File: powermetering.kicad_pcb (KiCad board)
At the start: 2 copper layers, 194 x 114.1 mm, 226 parts, among them J1 Conn_01x04, J16 Conn_02x20_Odd_Even, J2 Conn_01x02, J3 Conn_01x02, J4 Conn_01x02, J5 Conn_01x02, J6 HY951180A_RJ45, J7 CONN_01X02, J9 CONN_01X02, P2 CONN_01X04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

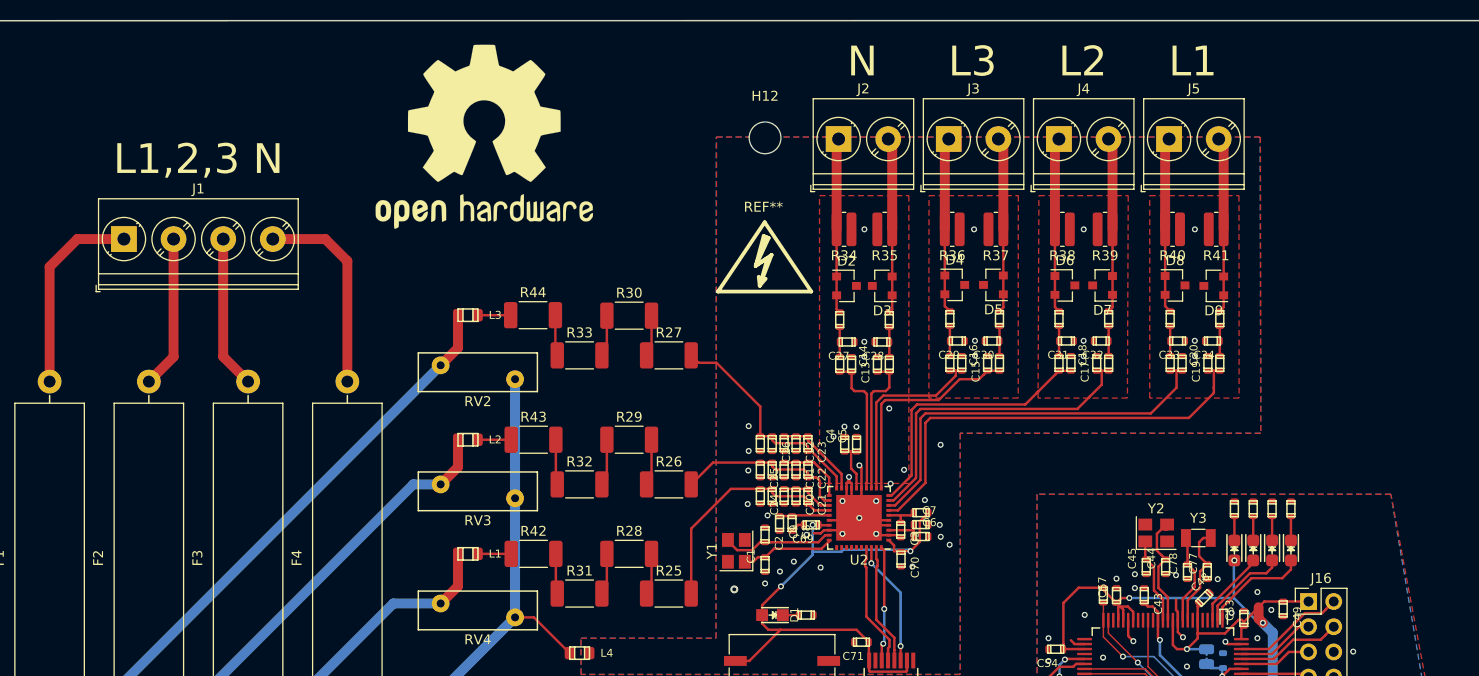
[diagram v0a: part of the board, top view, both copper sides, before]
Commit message: add EMI capacitor
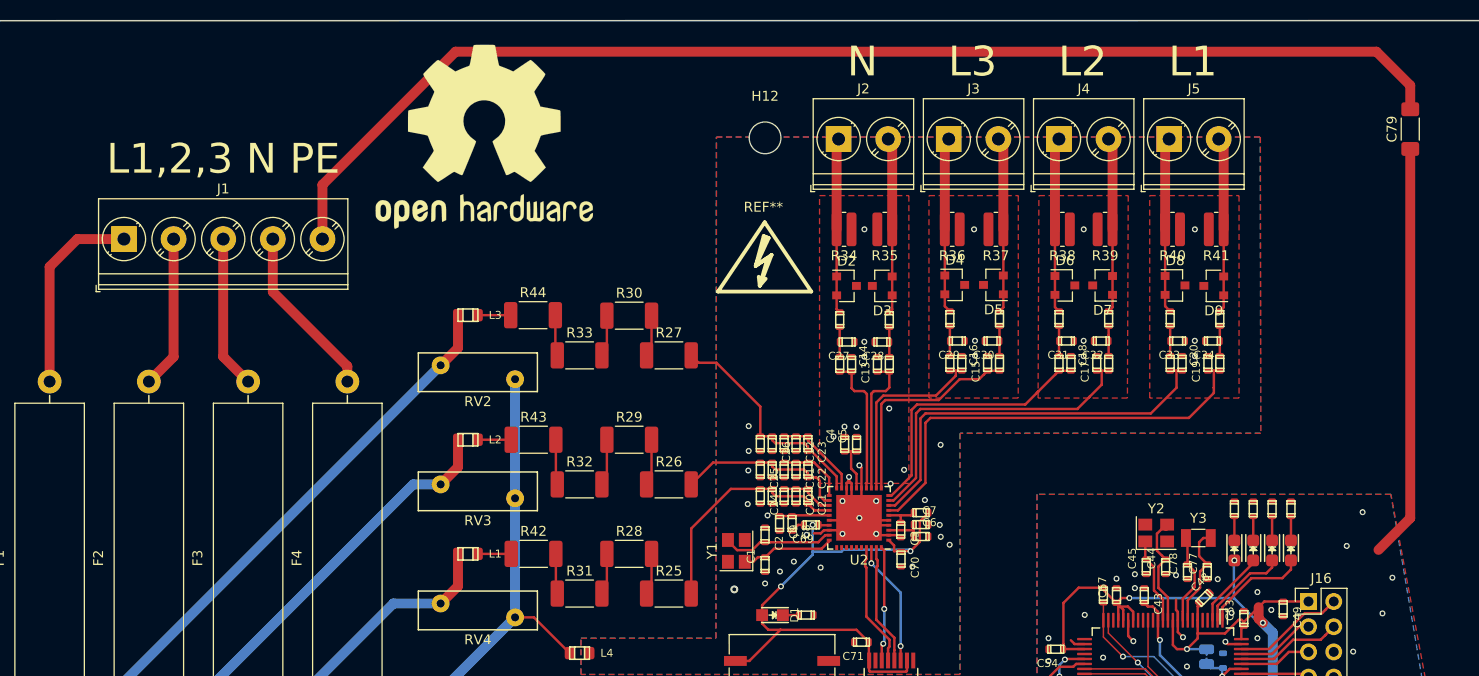
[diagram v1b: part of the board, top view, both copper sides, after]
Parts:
- added C79: C, Capacitor_SMD:C_1806_4516Metric, F.Cu at (265.0, 63.4)
- J1: footprint TerminalBlock_Phoenix:TerminalBlock_Phoenix_PT-1,5-4-5.0-H_1x04_P5.00mm_Horizontal -> TerminalBlock_Phoenix:TerminalBlock_Phoenix_PT-1,5-5-5.0-H_1x05_P5.00mm_Horizontal
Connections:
- net /phy_plug/PHY_CRS renamed /PHY_CRS
- net /phy_plug/PHY_INTRP renamed /PHY_INTRP
- net /phy_plug/PHY_MDC renamed /STM_MDC
- net /phy_plug/PHY_MDIO renamed /STM_MDIO
- net /phy_plug/PHY_REFCLK renamed /PHY_REFCLK
- net /phy_plug/PHY_RST renamed /PHY_RST
- net /phy_plug/PHY_RXD0 renamed /STM_RXD0
- net /phy_plug/PHY_RXD1 renamed /STM_RXD1
- net /phy_plug/PHY_TXD0 renamed /PHY_TXD0
- net /phy_plug/PHY_TXD1 renamed /STM_TXD1
- net /phy_plug/PHY_TXEN renamed /STM_TXEN
- net /phy_plug/PHY_X0 renamed /PHY_X0
- net /phy_plug/PHY_XI renamed /PHY_XI
- net /stm32/STM_MCO0 renamed /STM_MCO0
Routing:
- net Earth_Protective: track 0.00 -> 124.4 mm
- net GND: track 17.4 -> 59.2 mm, vias 92 -> 96
- net Net-(F4-Pad1): track 20.6 -> 17.5 mm
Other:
- board text added: "L1,2,3 N PE"
- board text removed: "L1,2,3 N"

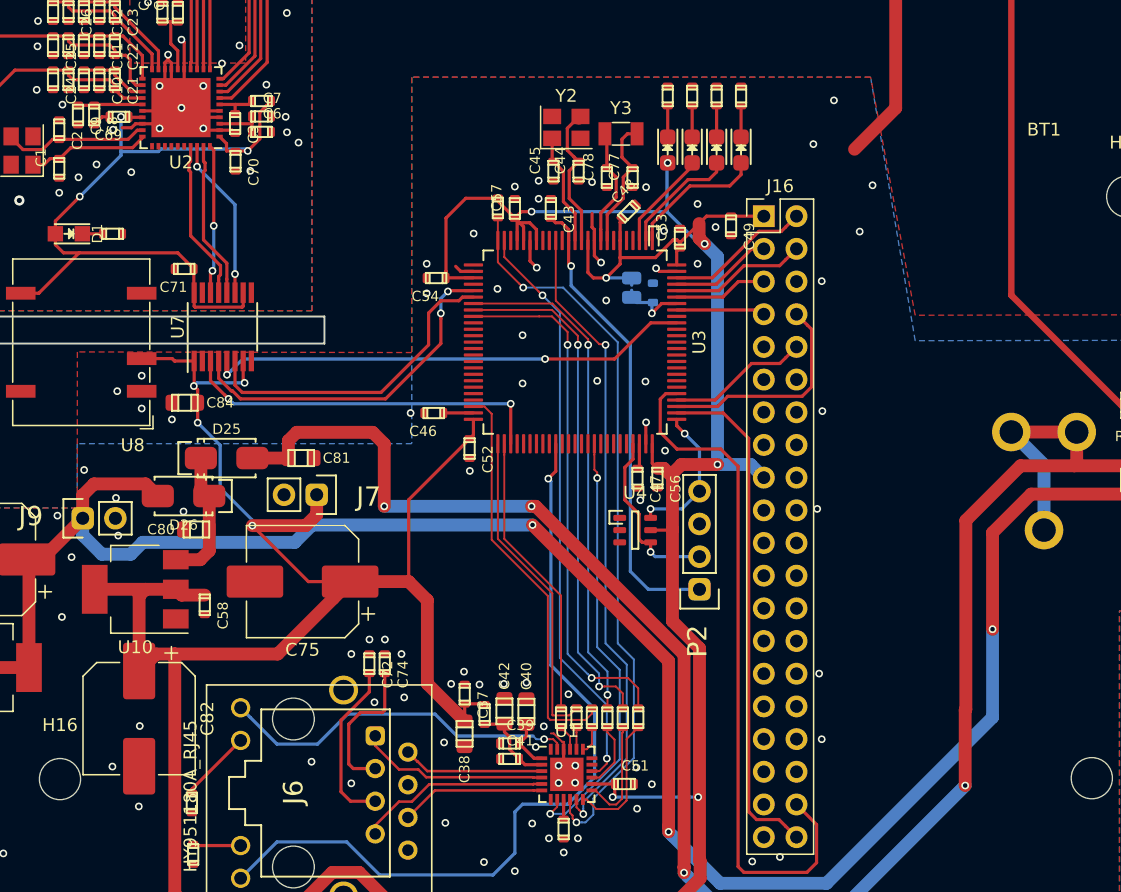
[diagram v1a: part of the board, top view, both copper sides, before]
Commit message: add sd card holder
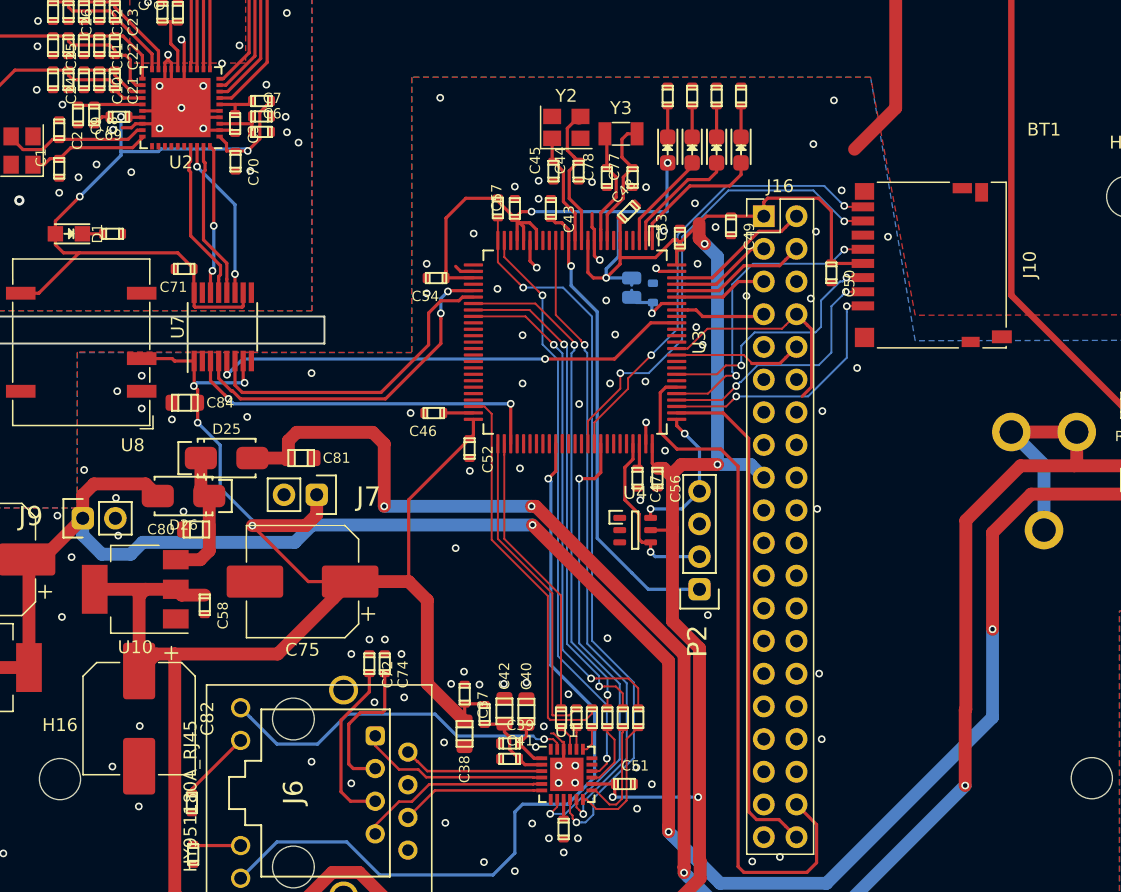
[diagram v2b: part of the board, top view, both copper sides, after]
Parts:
- added C50: 100n, stmbl:C_0603, F.Cu at (260.0, 115.4)
- added J10: Micro_SD_Card, Connector_Card:microSD_HC_Hirose_DM3D-SF, F.Cu at (267.8, 114.8)
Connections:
- net /PHY_REFCLK renamed /STM_REFCLK
- U1 pad 8: /PHY_XI -> /STM_MCO0
- U3 pad 66: /PHY_XI -> Net-(J10-Pad8)
- U3 pad 78: USART3_TX -> Net-(J10-Pad1)
- U3 pad 79: USART3_RX -> Net-(J10-Pad2)
- U3 pad 80: MMDVM_BOOT0 -> Net-(J10-Pad5)
- U3 pad 81: Net-(U3-Pad81) -> MMDVM_BOOT0
- U3 pad 86: Net-(U3-Pad86) -> USART3_RX
- U3 pad 87: Net-(U3-Pad87) -> USART3_TX
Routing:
- net Net-(J10-Pad7): track 0.00 -> 37.0 mm, vias 0 -> 2
- net /STM_MCO0: track 0.00 -> 35.7 mm, vias 0 -> 2
- net Net-(J10-Pad8): track 0.00 -> 35.6 mm, vias 0 -> 2
- net /PHY_XI: track 33.8 -> 0.00 mm, vias 2 -> 0
- net Net-(J10-Pad5): track 0.00 -> 23.7 mm, vias 0 -> 2
- net Net-(J10-Pad2): track 0.00 -> 20.1 mm, vias 0 -> 2
- net Net-(J10-Pad1): track 0.00 -> 20.1 mm, vias 0 -> 2
- net Net-(J10-Pad3): track 0.00 -> 19.7 mm, vias 0 -> 2
- net +3V3: track 313.1 -> 328.6 mm
- net /STM_RXD1: track 41.0 -> 39.8 mm
- net /STM_RXD0: track 40.1 -> 39.1 mm
- net USART3_RX: track 11.0 -> 10.1 mm
- net /PHY_CRS: track 39.4 -> 38.8 mm
- net MMDVM_BOOT0: track 54.1 -> 54.6 mm
- net GND: vias 96 -> 110

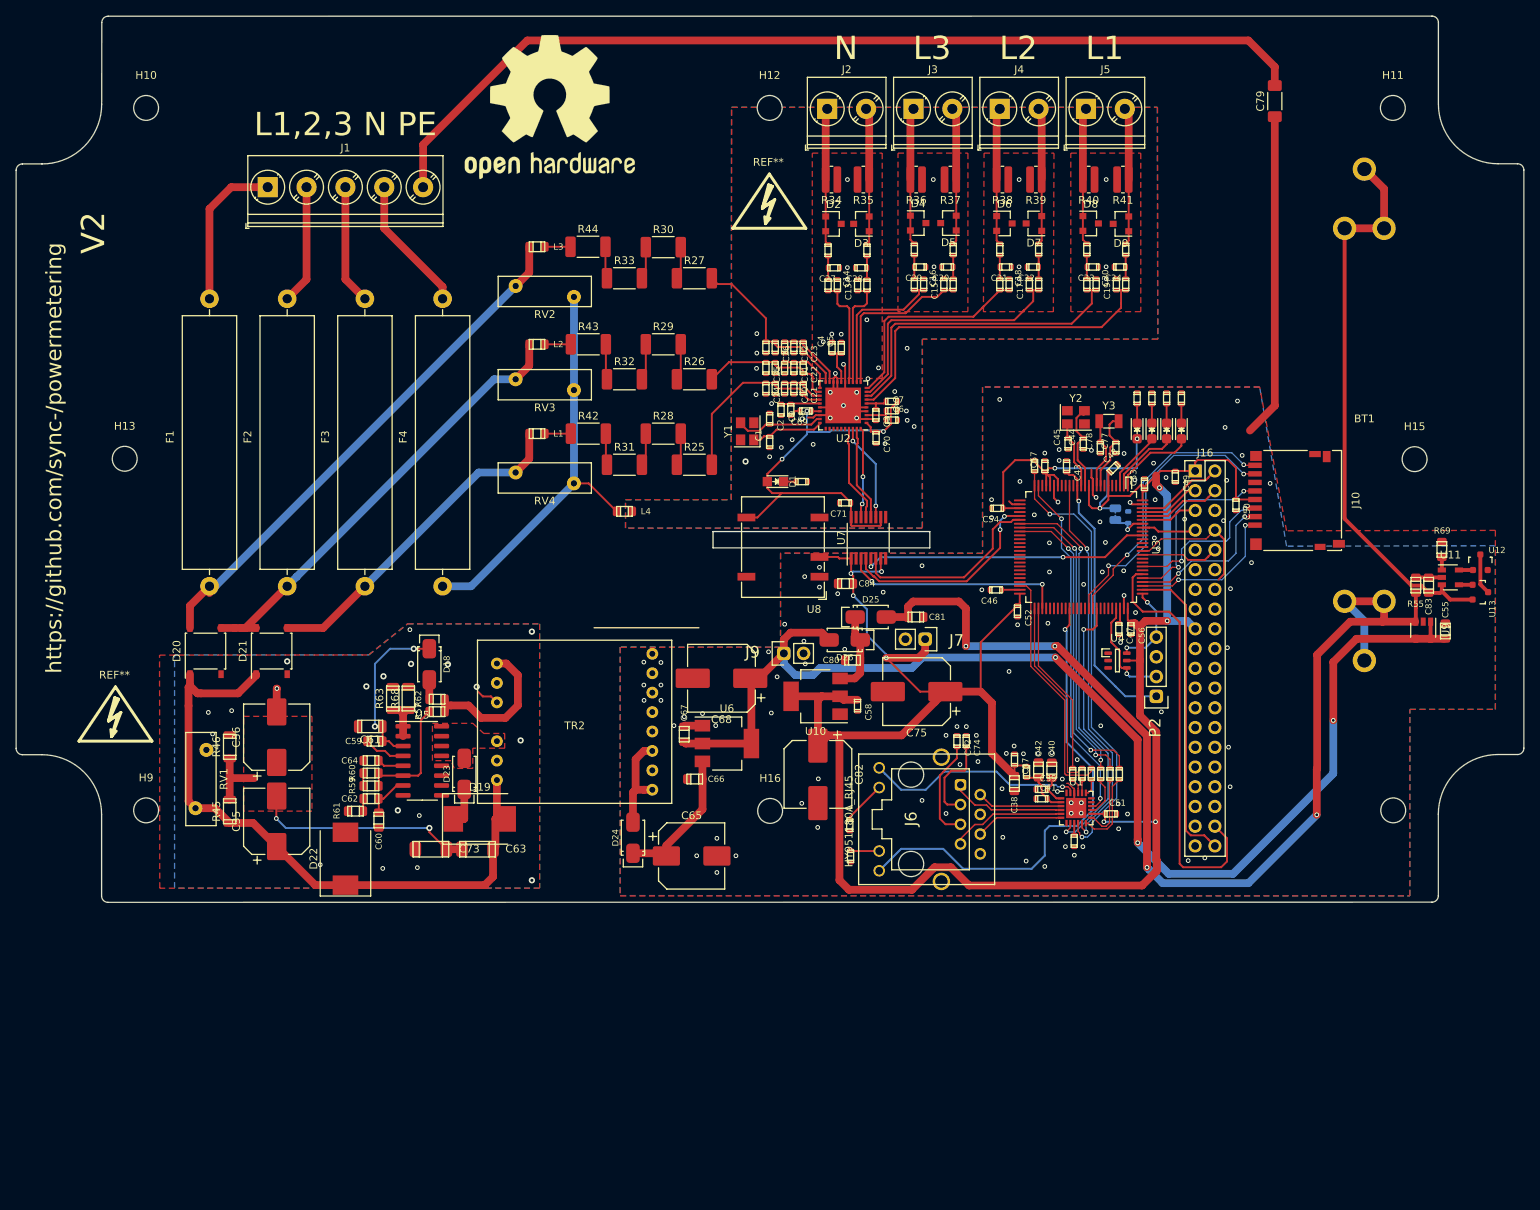
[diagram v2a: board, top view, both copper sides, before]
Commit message: add bodge pads and move stuff around
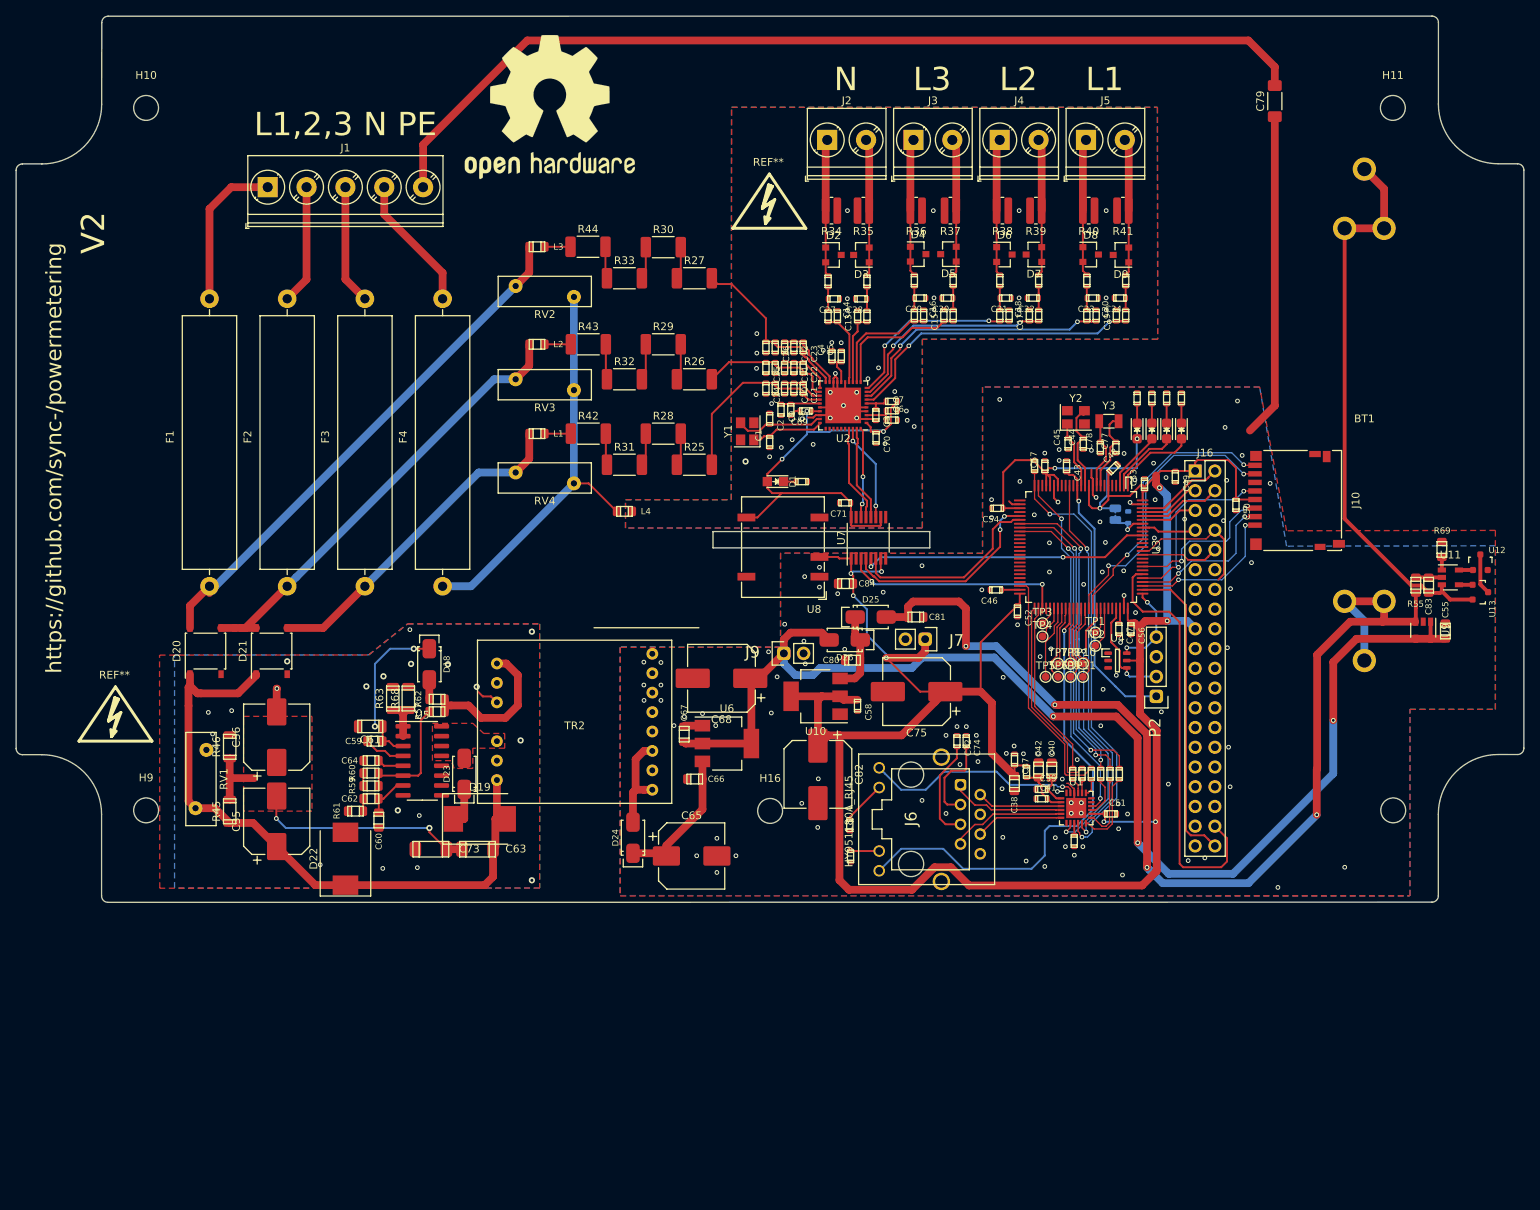
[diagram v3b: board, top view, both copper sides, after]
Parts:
- removed H12, H13, H15: MountingHole, MountingHole:MountingHole_3.2mm_M3
- added TP1: TestPoint, TestPoint:TestPoint_Pad_D1.0mm, F.Cu at (241.9, 131.8)
- added TP10: TestPoint, TestPoint:TestPoint_Pad_D1.0mm, F.Cu at (240.3, 135.8)
- added TP11: TestPoint, TestPoint:TestPoint_Pad_D1.0mm, F.Cu at (240.3, 137.5)
- added TP2: TestPoint, TestPoint:TestPoint_Pad_D1.0mm, F.Cu at (241.9, 133.5)
- added TP3: TestPoint, TestPoint:TestPoint_Pad_D1.0mm, F.Cu at (235.1, 130.6)
- added TP4: TestPoint, TestPoint:TestPoint_Pad_D1.0mm, F.Cu at (235.1, 132.3)
- added TP5: TestPoint, TestPoint:TestPoint_Pad_D1.0mm, F.Cu at (235.5, 137.5)
- added TP6: TestPoint, TestPoint:TestPoint_Pad_D1.0mm, F.Cu at (237.1, 137.5)
- added TP7: TestPoint, TestPoint:TestPoint_Pad_D1.0mm, F.Cu at (237.1, 135.8)
- added TP8: TestPoint, TestPoint:TestPoint_Pad_D1.0mm, F.Cu at (238.7, 135.8)
- added TP9: TestPoint, TestPoint:TestPoint_Pad_D1.0mm, F.Cu at (238.7, 137.5)
- moved C13 4.00 mm to (208.7, 91.1)
- moved C14 4.00 mm to (211.3, 91.1)
- moved C15 4.00 mm to (219.8, 91.0)
- moved C16 4.00 mm to (222.4, 91.0)
- moved C17 4.00 mm to (230.8, 91.0)
- moved C18 4.00 mm to (233.4, 91.0)
- moved C19 4.00 mm to (242.0, 91.0)
- moved C20 4.00 mm to (244.6, 91.0)
- moved C27 4.00 mm to (208.3, 88.8)
- moved C28 4.00 mm to (211.8, 88.8)
- moved C29 4.00 mm to (219.4, 88.8)
- moved C30 4.00 mm to (222.9, 88.8)
- moved C31 4.00 mm to (230.4, 88.8)
- moved C32 4.00 mm to (233.9, 88.8)
- moved C33 4.00 mm to (241.6, 88.8)
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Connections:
- net /PHY_CRS renamed /STM_CRS
- net /STM_MCO0 renamed /PHY_XI
- net /STM_MDC renamed /PHY_MDC
- net /STM_MDIO renamed /PHY_MDIO
- net /STM_REFCLK renamed /PHY_REFCLK
- net /STM_RXD0 renamed /PHY_RXD0
- net /STM_RXD1 renamed /PHY_RXD1
- net /STM_TXD1 renamed /PHY_TXD1
- net /STM_TXEN renamed /PHY_TXEN
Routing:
- net Net-(TP11-Pad1): track 0.00 -> 10.5 mm
- net Net-(TP9-Pad1): track 0.00 -> 9.65 mm
- net Net-(TP6-Pad1): track 0.00 -> 9.65 mm
- net Net-(TP5-Pad1): track 0.00 -> 9.46 mm
- net Net-(TP10-Pad1): track 0.00 -> 7.89 mm
- net Net-(TP7-Pad1): track 0.00 -> 7.52 mm
- net Net-(TP8-Pad1): track 0.00 -> 7.39 mm
- net /IL1P: track 44.7 -> 38.9 mm, vias 0 -> 2
- net /IL1N: track 40.5 -> 35.2 mm, vias 0 -> 2
- net Net-(TP2-Pad1): track 0.00 -> 5.30 mm
- net /INP: track 14.4 -> 9.17 mm
- net /IL2P: track 32.8 -> 27.6 mm, vias 0 -> 2
- net /IL3N: track 19.4 -> 14.8 mm
- net /INN: track 14.1 -> 9.57 mm
- net Net-(TP4-Pad1): track 0.00 -> 4.22 mm
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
